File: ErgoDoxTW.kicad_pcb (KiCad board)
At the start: 2 copper layers, 182.8 x 158.9 mm, 74 parts, among them J2 3.5mm, J3 JMP, J4 JMP, P1 hole_r1.75, P2 hole_r1.75, P3 hole_r1.75, P4 hole_r1.75, P5 hole_r1.75, P6 hole_r1.75, P7 hole_r1.75, P8 hole_r1.75, SW0:10 SW0:3, SW0:11 SW0:2, SW0:12 SW0:1, SW0:7 SW0:6, SW0:8 SW0:5, SW0:9 SW0:4, SW1:10 SW1:3, SW1:11 SW1:2, SW1:12 SW1:1, SW1:13 SW1:0, SW1:9 SW1:4, SW2:10 SW2:3, SW2:11 SW2:2, SW2:12 SW2:1, SW2:13 SW2:0, SW2:7 SW2:6, SW2:8 SW2:5, SW2:9 SW2:4, SW3:10 SW3:3, SW3:11 SW3:2, SW3:12 SW3:1, SW3:13 SW3:0, SW3:8 SW3:5, SW3:9 SW3:4, SW4:10 SW4:3, SW4:11 SW4:2, SW4:12 SW4:1, SW4:13 SW4:0, SW4:7 SW4:6, SW4:8 SW4:5, SW4:9 SW4:4, SW5:10 SW5:3, SW5:11 SW5:2, SW5:12 SW5:1, SW5:13 SW5:0, SW5:7 SW5:6, SW5:8 SW5:5, SW5:9 SW5:4, U2 MCP23018, U4 TEENSY2.0

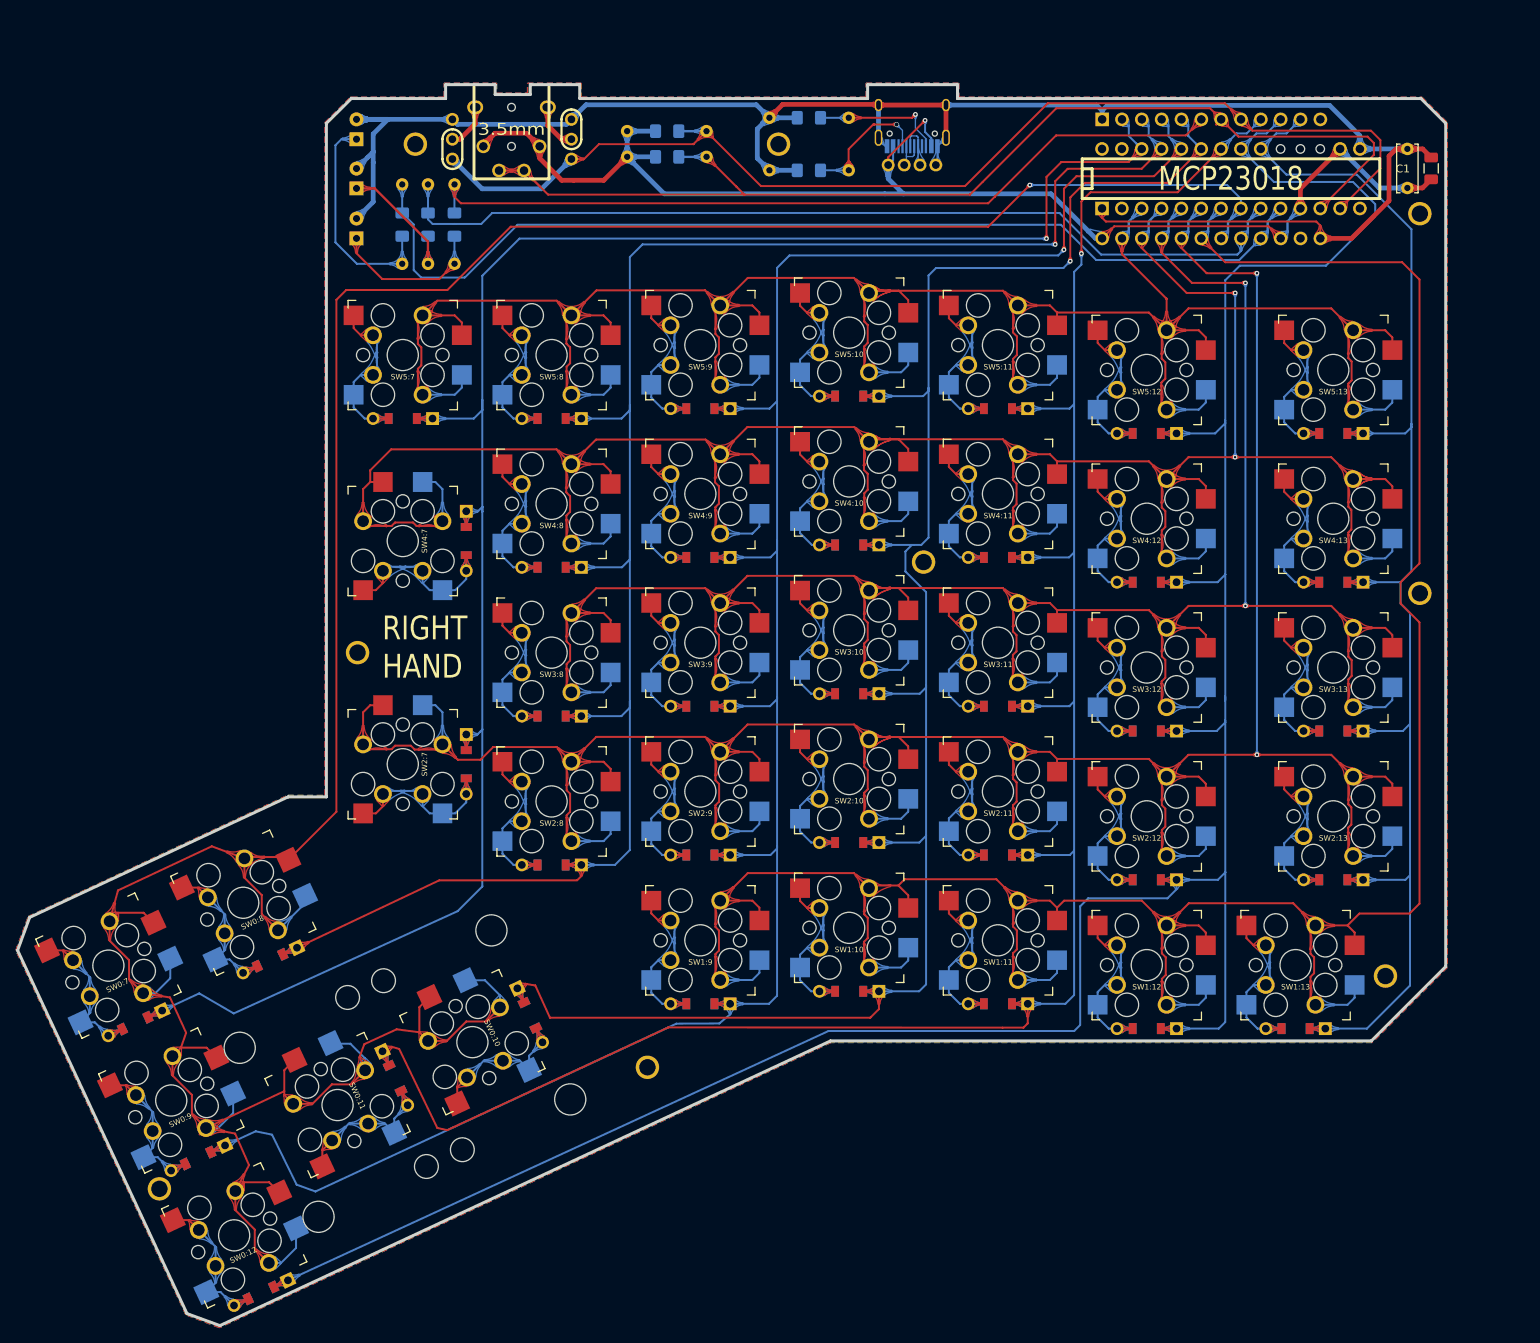
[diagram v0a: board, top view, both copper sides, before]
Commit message: update v1.0
1. Change USB VCC trace to 0.609 mm
2. Make all via larger
3. reroute the trace in thumb area
4. add some pcb text
5. update README.md
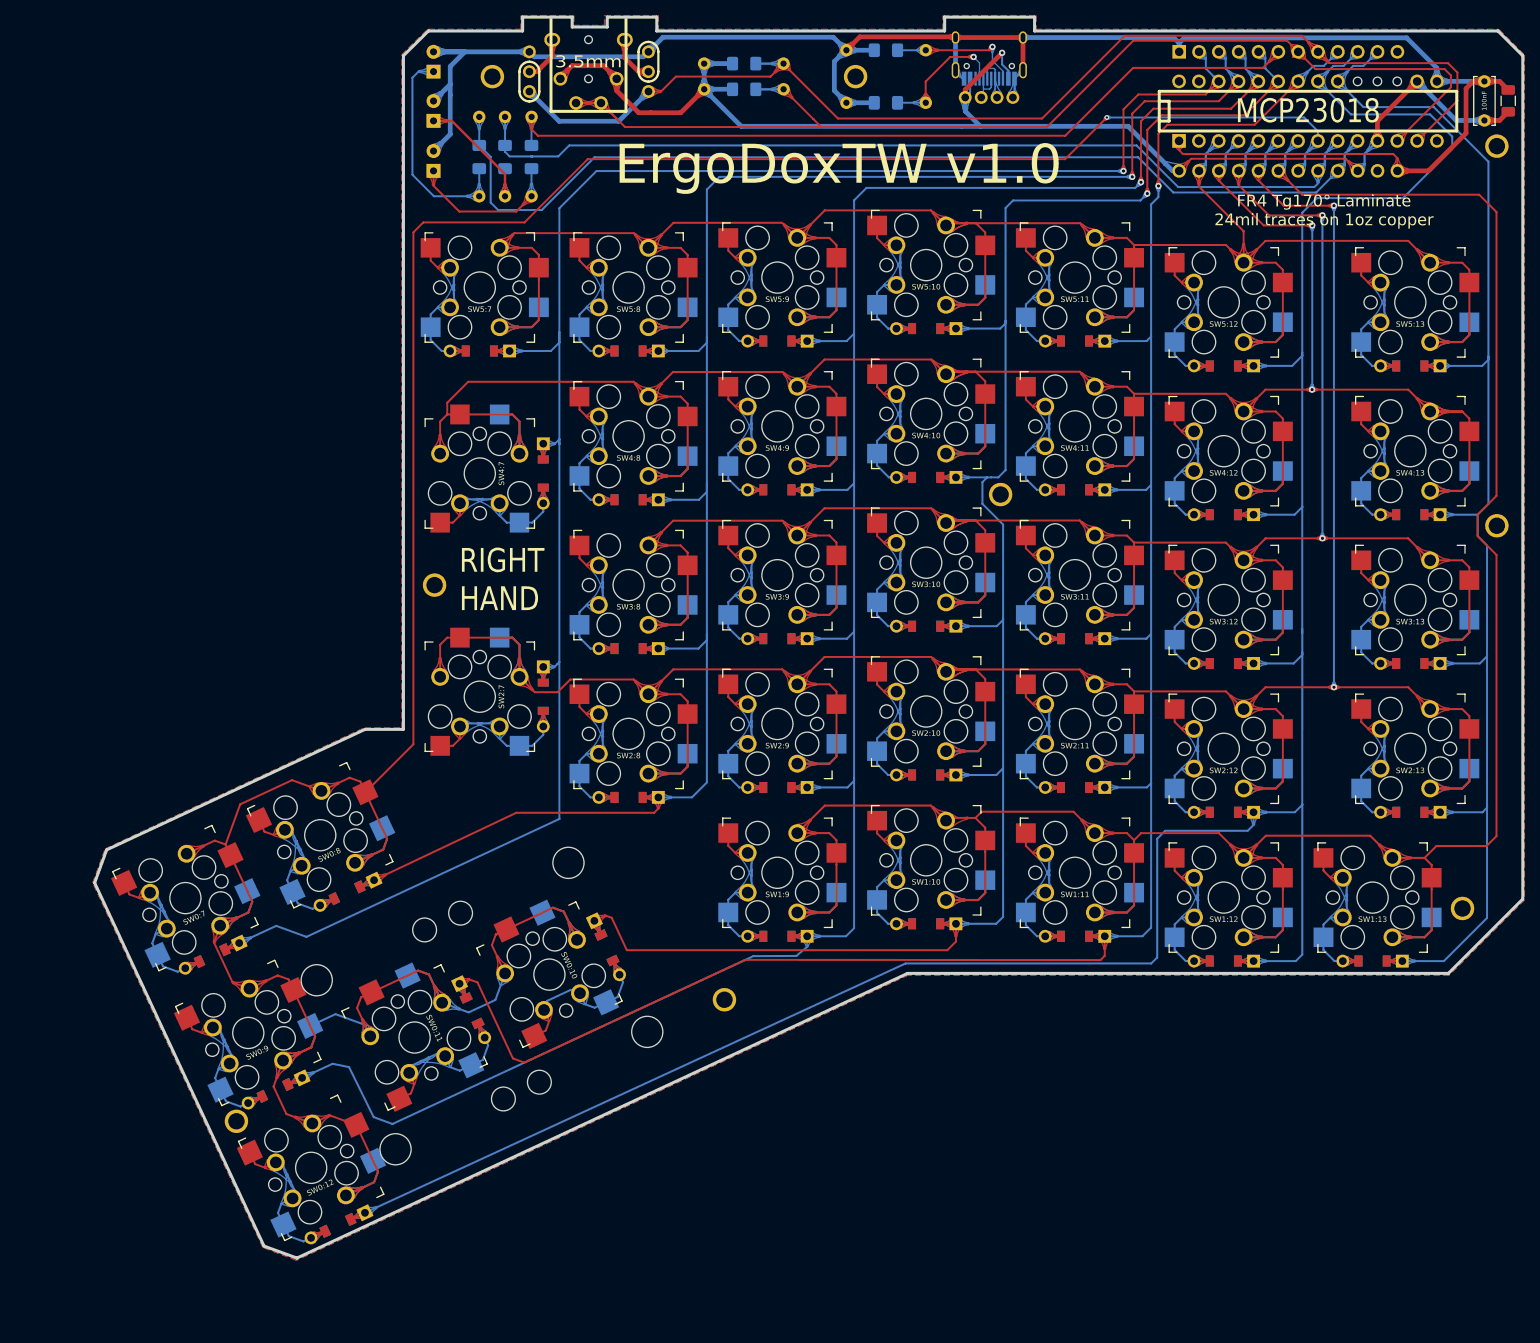
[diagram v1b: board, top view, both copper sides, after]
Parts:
- moved P4 13.1 mm to (208.1, 136.0)
- moved SW4:13 13.1 mm to (201.4, 77.4)
- moved SW3:11 13.1 mm to (158.5, 93.3)
- moved SW1:9 13.1 mm to (120.4, 131.4)
- moved SW5:10 13.1 mm to (139.4, 53.6)
- moved RB2 13.1 mm to (85.5, 39.7)
- moved SW3:13 13.1 mm to (201.4, 96.5)
- moved SW4:11 13.1 mm to (158.5, 74.2)
- moved U2 13.1 mm to (188.3, 33.9)
- moved R1 13.1 mm to (111.0, 27.8)
- moved SW4:10 13.1 mm to (139.4, 72.6)
- moved SW5:12 13.1 mm to (177.5, 58.4)
- moved P5 13.1 mm to (212.5, 87.0)
- moved SW2:13 13.1 mm to (201.4, 115.5)
- moved R6 13.1 mm to (116.1, 31.1)
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- renumbered C1 to 100nF
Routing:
- net /ROW2: track 376.6 -> 384.1 mm
- net /ROW4: track 353.9 -> 361.3 mm
- net /ROW5: track 318.9 -> 326.2 mm
- net /ROW3: track 314.4 -> 320.8 mm
- net /ROW0: track 416.7 -> 422.3 mm
- net /ROW1: track 328.5 -> 333.7 mm
- net /COL10: track 256.4 -> 254.2 mm
- net Net-(SW0:10-Pad2): track 22.0 -> 24.1 mm
- net Net-(SW0:8-Pad2): track 22.0 -> 24.0 mm
- net Net-(SW0:11-Pad2): track 22.0 -> 24.0 mm
- net Net-(SW0:12-Pad2): track 22.0 -> 23.9 mm
- net Net-(SW0:9-Pad2): track 22.0 -> 23.9 mm
- net Net-(SW0:7-Pad2): track 22.0 -> 23.9 mm
- net /COL6: track 257.8 -> 256.6 mm
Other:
- board text added: "ErgoDoxTW v1.0"
- board text added: "FR4 Tg170° Laminate 24mil traces on 1oz copper"

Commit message: update to v1.2
1. change 3.5mm audio socket component to PJ-320A (pin on right side)
and PJ-320L (pin on left side)
2. change key switch layout
3. change
trace to 0.609 mm for key switch (due to above)
4. fix some typo
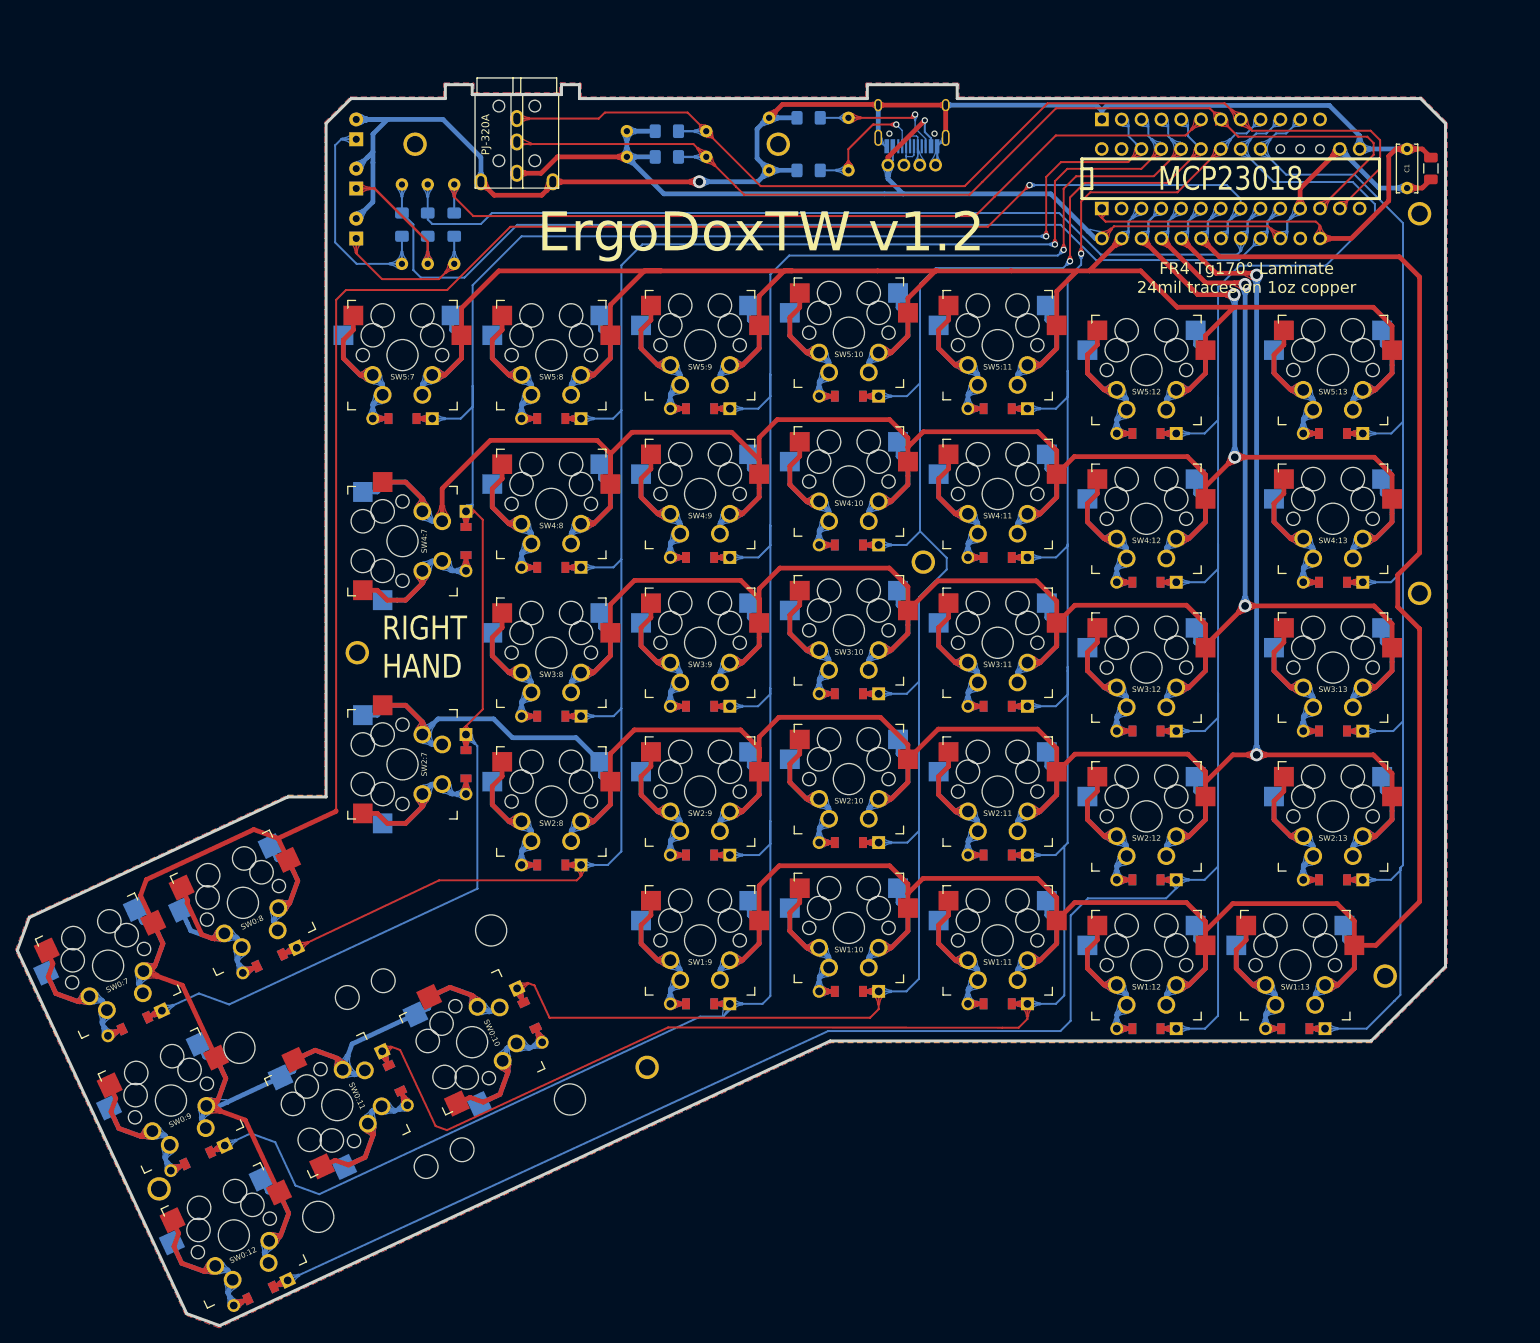
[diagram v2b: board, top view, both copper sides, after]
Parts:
- removed J2: 3.5mm, ErgoDone:4pin35mmAudio
- removed J3, J4: JMP, ErgoDone:100PITCH1X3
- added J1: 3.5mm, Enhance:PJ-320A-Dual, F.Cu at (87.0, 31.6)
- SW0:10, SW0:11, SW0:12, SW0:7, SW0:8, SW0:9, SW1:10, SW1:11, SW1:12, SW1:13, SW1:9, SW2:10, SW2:11, SW2:12, SW2:13, SW2:7, SW2:8, SW2:9, SW3:10, SW3:11, SW3:12, SW3:13, SW3:8, SW3:9, SW4:10, SW4:11, SW4:12, SW4:13, SW4:7, SW4:8, SW4:9, SW5:10, SW5:11, SW5:12, SW5:13, SW5:7, SW5:8, SW5:9: footprint Enhance:Kailh_socket_optional_reversible_diode_smd -> Enhance:Kailh_socket_diode_smd
- moved P6 13.1 mm to (202.6, 47.0)
- moved SW3:12 13.1 mm to (167.6, 105.1)
- moved SW3:13 13.1 mm to (191.5, 105.1)
- moved SW3:8 13.1 mm to (91.4, 103.2)
- moved SW4:11 13.1 mm to (148.6, 82.9)
- moved SW4:7 13.1 mm to (72.4, 88.9)
- moved SW5:9 13.1 mm to (110.5, 63.8)
- moved RB2 13.1 mm to (75.6, 48.4)
- moved RC2 13.1 mm to (79.0, 48.4)
- moved SW5:8 13.1 mm to (91.4, 65.1)
- moved SW2:11 13.1 mm to (148.6, 121.0)
- moved R8 13.1 mm to (124.3, 34.7)
- moved LED2 13.1 mm to (66.4, 43.8)
- moved S2 13.1 mm to (81.3, 153.1)
- moved SW0:10 13.1 mm to (81.3, 153.1)
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- renumbered 100nF to C1
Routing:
- net /SDAM: track 147.2 -> 135.6 mm
- net /ROW0: track 422.3 -> 412.4 mm
- net /COL5: track 251.9 -> 242.6 mm
- net VCC: track 170.9 -> 162.0 mm
- net /ROW5: track 326.2 -> 333.9 mm
- net /SCLM: track 143.2 -> 135.5 mm
- net Net-(J2-Pad1): track 6.08 -> 0.00 mm
- net Net-(J2-Pad4): track 5.86 -> 0.00 mm
- net Net-(SW2:7-Pad2): track 23.7 -> 28.9 mm
- net GND: track 247.3 -> 252.5 mm, vias 0 -> 1
- net Net-(SW4:10-Pad2): track 23.7 -> 28.9 mm
- net Net-(SW5:7-Pad2): track 23.8 -> 28.9 mm
- net Net-(SW5:9-Pad2): track 23.8 -> 28.9 mm
- net Net-(SW4:12-Pad2): track 23.8 -> 28.9 mm
- net Net-(SW4:13-Pad2): track 23.8 -> 28.9 mm
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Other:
- outline, holes or cut-outs redrawn
- board text added: "ErgoDoxTW v1.2"
- board text removed: "ErgoDoxTW v1.0"

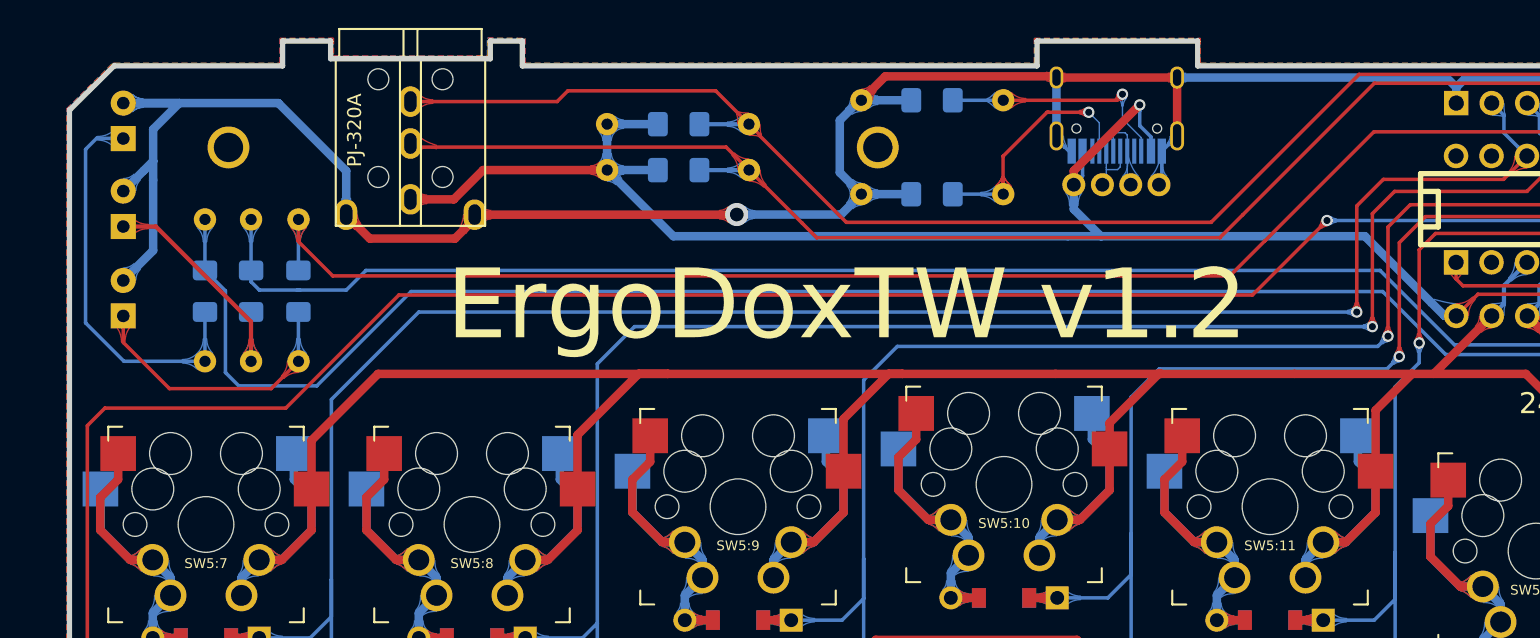
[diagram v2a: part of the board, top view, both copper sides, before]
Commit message: update v1.2.1
Main change :
1. fix 3.5mm audio jack position

Minor change:
1. add key_switch / stabilizer 3d models for preview
2. add full pcb preview image
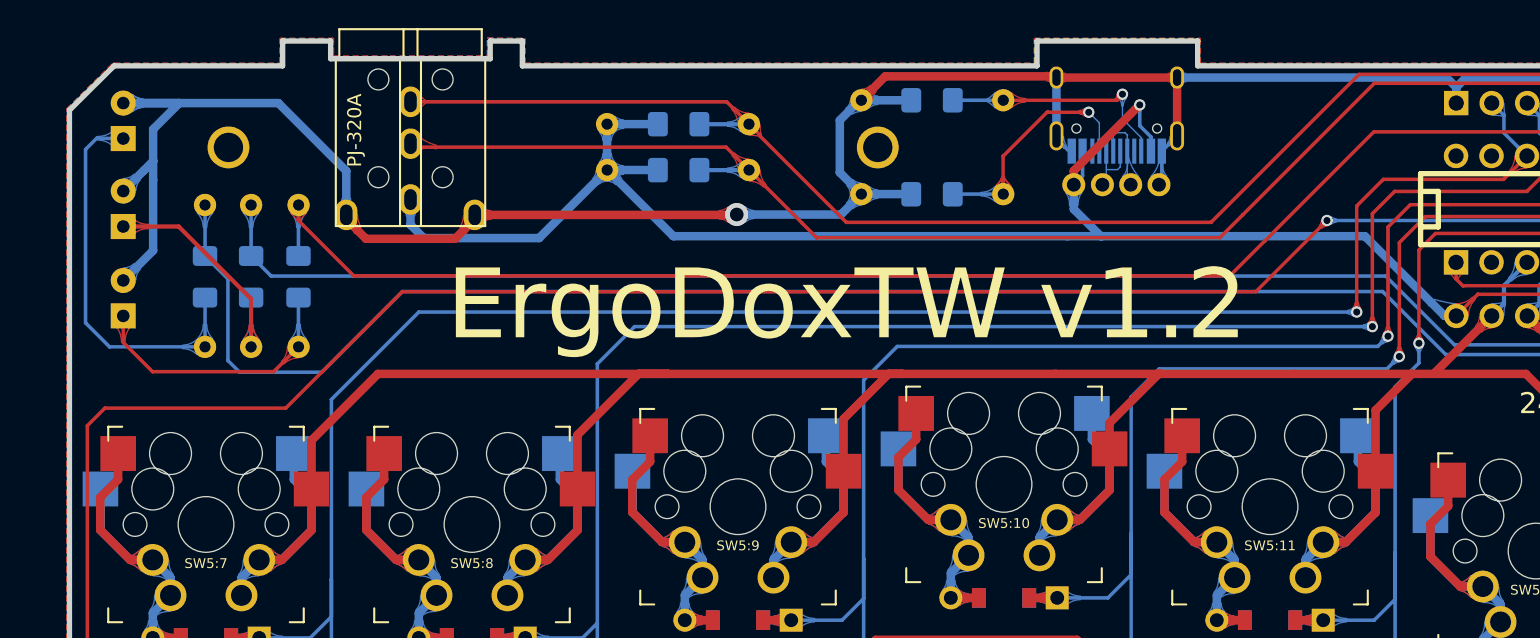
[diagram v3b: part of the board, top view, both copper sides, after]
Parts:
- moved RA1 1.03 mm to (72.3, 42.2)
- moved RA2 1.03 mm to (72.3, 47.4)
- moved RB1 1.03 mm to (75.6, 42.2)
- moved RB2 1.03 mm to (75.6, 47.4)
- moved RC1 1.03 mm to (79.0, 42.2)
- moved RC2 1.03 mm to (79.0, 47.4)
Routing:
- net VCC: track 162.0 -> 165.3 mm
- net /LED_B: track 118.5 -> 117.1 mm
- net /LED_C: track 107.1 -> 108.3 mm
- net /SDAM: track 135.6 -> 134.9 mm
- net Net-(LED3-Pad1): track 20.2 -> 19.6 mm
